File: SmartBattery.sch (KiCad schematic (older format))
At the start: 12 parts, among them J16 Conn_01x03_Female, J17 Conn_01x03_Female, J18 Conn_01x03_Female, J2 ST-USB-003A, Q22 AO3401A, U13 TPS2511DGNR, U14 HT7533-1

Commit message: Type_A_implemented. Sch "locked". PCB Layout started.
*Changelog:
*Type-a switching regulator (TBD -- need to check inductor,caps, stability. Maybe check both peripherial inductors?)
*Type-A load switch + connector + esd
*started layout..
*found out that my footprint for n fet is wrong. Fixing now, need to replace all of those.
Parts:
- removed J16, J17, J18: Conn_01x03_Female, symbol Connector:Conn_01x03_Female
- removed J2: ST-USB-003A, Connector_USB:USB3_A_Plug_Wuerth_692112030100_Horizontal, symbol Connector:USB_B
- removed U13: TPS2511DGNR, SmartBattery:SOP65P490X110-9N, symbol SmartBattery:TPS2511DGNR
- added H1, H2, H3: MountingHole, SmartBattery:MountingHole_1.152mm_JLPCB, symbol Mechanical:MountingHole
- added H4, H5, H6: MountingHole, MountingHole:MountingHole_2.2mm_M2, symbol Mechanical:MountingHole
- added J12: Conn_01x10_Male, Connector_PinHeader_1.27mm:PinHeader_2x05_P1.27mm_Vertical_SMD, symbol Connector:Conn_01x10_Male
- added J?: Conn_01x03_Male, Connector_PinHeader_2.54mm:PinHeader_1x03_P2.54mm_Vertical, symbol Connector:Conn_01x03_Male
- added TP46, TP47, TP48, TP49, TP50, TP51, TP55: TestPoint_Flag, TestPoint:TestPoint_Pad_3.0x3.0mm, symbol Connector:TestPoint_Flag
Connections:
- wire segments 22 -> 20

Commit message: Much layout. Wow
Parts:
- gave numbers to parts that had none: 1
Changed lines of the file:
@@
 $EndComp
 $Comp
-L Connector:Conn_01x03_Male J?
+L Connector:Conn_01x03_Male J13
 U 1 1 604AF604
 P 5300 2300
-F 0 "J?" H 5408 2581 50  0000 C CNN
+F 0 "J13" H 5408 2581 50  0000 C CNN
 F 1 "Conn_01x03_Male" H 5408 2490 50  0000 C CNN
 F 2 "Connector_PinHeader_2.54mm:PinHeader_1x03_P2.54mm_Vertical" H 5300 2300 50  0001 C CNN

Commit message: Much layout wow.
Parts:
- removed J12: Conn_01x10_Male, Connector_PinHeader_1.27mm:PinHeader_2x05_P1.27mm_Vertical_SMD, symbol Connector:Conn_01x10_Male
- added R110, R62, R63: 100k, lc_lib:0402_R, symbol Device:R_Small_US
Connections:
- net Barrel_Jack_Input/BARREL_RAW: now also D12.2 (A)
- net GND: now also C112.1, C113.1, U14.1 (GND), R62.2
- net at U14.2 (VIN): now also C112.2, D12.1 (K), D14.1 (K)
- net at U14.3 (VOUT): now also C113.2, D13.2 (A)
- net +3.3VP: now reaches D13.1 (K)
- net +3.3VP: now also Q22.2 (S), R110.2
- net type_c_input/INPUT_TYPEC_VBUS_RAW: now reaches D14.2 (A)
- net at Q22.1 (G): now also R110.1
- net Peripheral_3p3v/3p3v: now reaches Q22.3 (D)
- new net: R62.1, R63.1
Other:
- note added: "TOOLING HOLE\n"
- note added: "m.2 hole\n"
- moved on the sheet: C112, C113, D12, D13, D14, Q22, U14

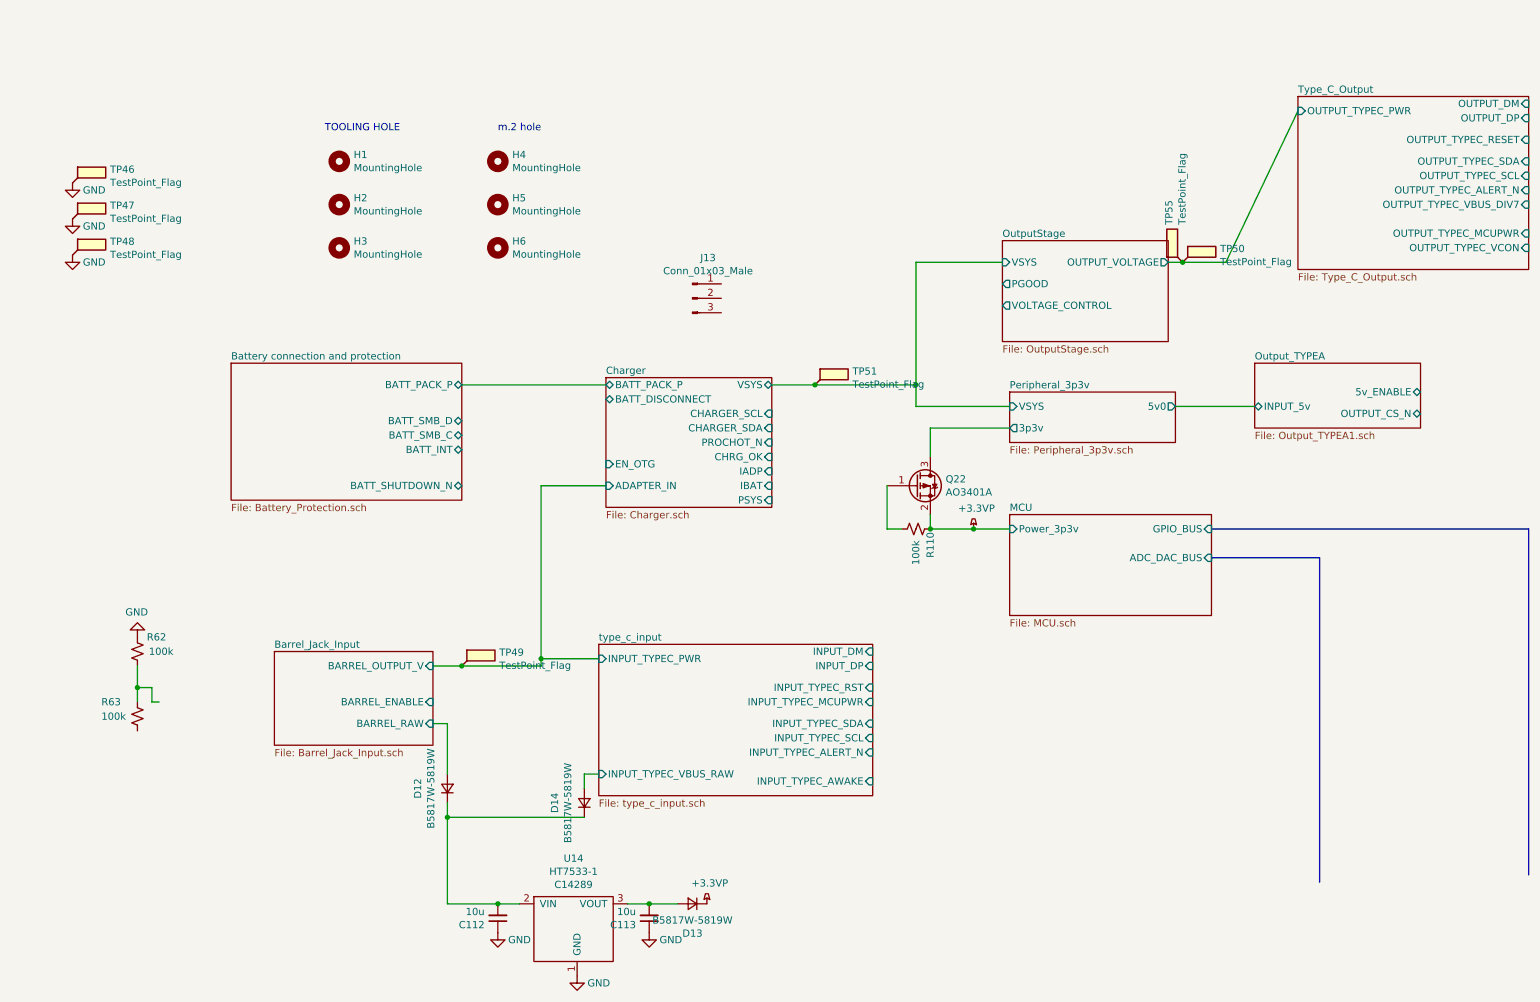
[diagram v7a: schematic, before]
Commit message: Almost connected MCU + ESP32 added leds addedd uart usb cleaned up type-c I/O -- STILL NEED TO level shift I2C
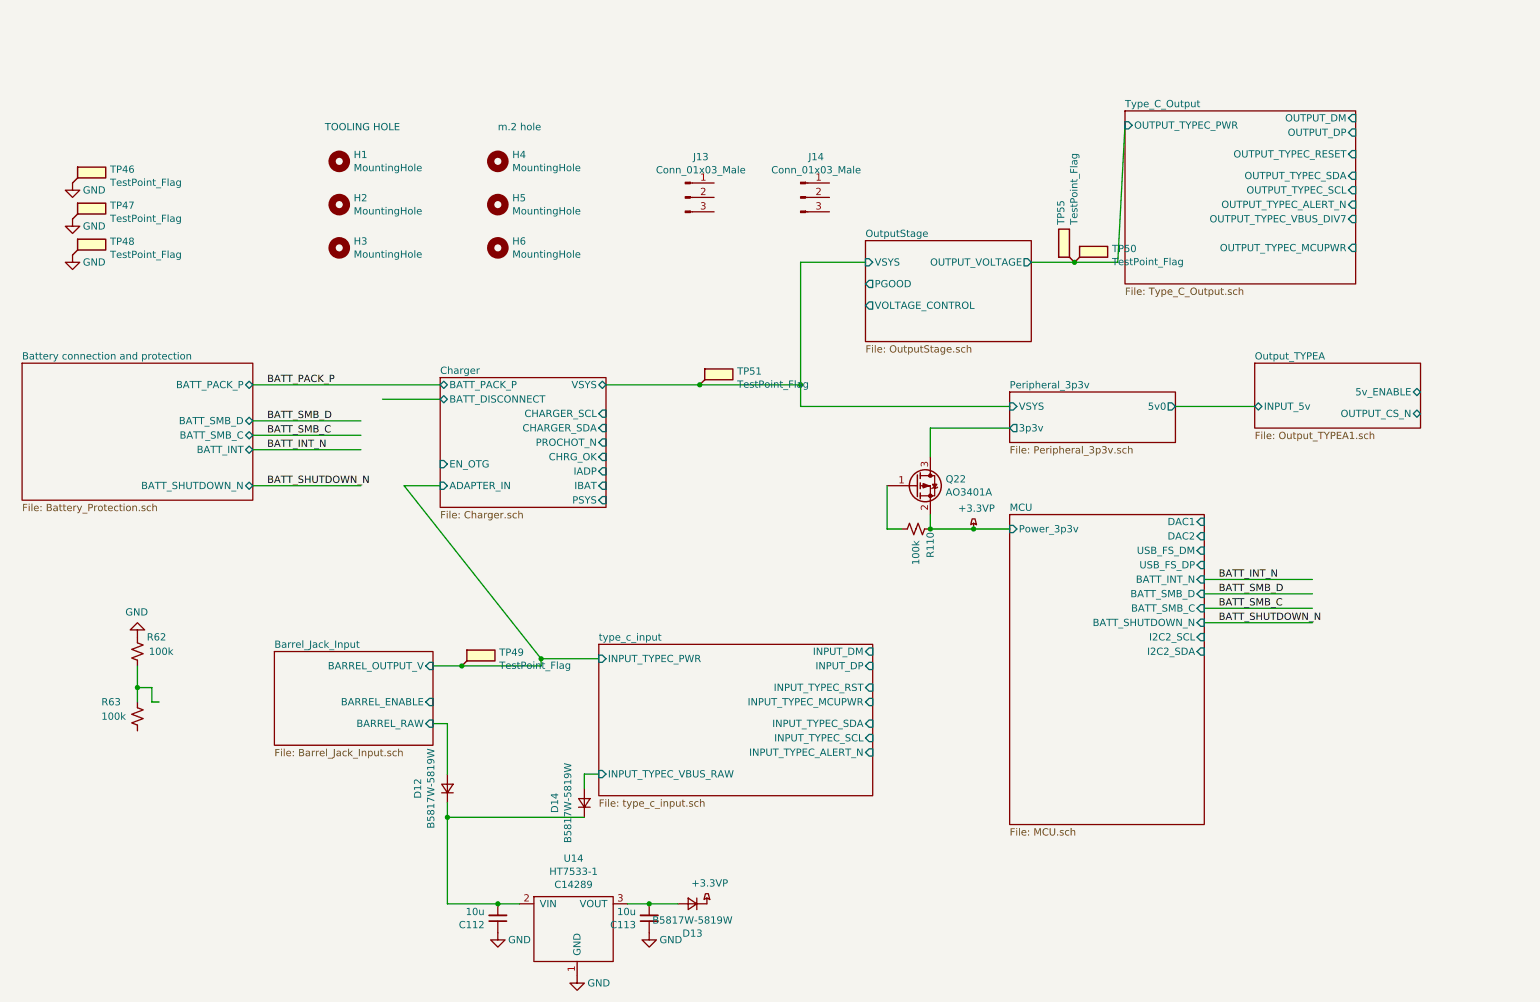
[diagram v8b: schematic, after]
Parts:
- added J14: Conn_01x03_Male, Connector_PinHeader_2.54mm:PinHeader_1x03_P2.54mm_Vertical, symbol Connector:Conn_01x03_Male
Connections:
- net labels added: BATT_INT_N, BATT_PACK_P, BATT_SHUTDOWN_N, BATT_SMB_C, BATT_SMB_D
- wire segments 40 -> 49
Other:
- moved on the sheet: J13, TP50, TP51, TP55
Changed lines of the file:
@@
 $EndDescr
 $Sheet
-S 4700 2850 1150 900
+S 3550 2850 1150 900
 U 5FD99B08
 F0 "Charger" 50
 F1 "Charger.sch" 50
-F2 "BATT_PACK_P" B L 4700 2900 50
-F3 "VSYS" B R 5850 2900 50
-F4 "IBAT" I R 5850 3600 50
-F5 "IADP" I R 5850 3500 50
-F6 "PROCHOT_N" I R 5850 3300 50
-F7 "CHARGER_SDA" I R 5850 3200 50
-F8 "CHARGER_SCL" I R 5850 3100 50
-F9 "ADAPTER_IN" I L 4700 3600 50
-F10 "PSYS" I R 5850 3700 50
-F11 "CHRG_OK" I R 5850 3400 50
-F12 "EN_OTG" I L 4700 3450 50
-F13 "BATT_DISCONNECT" B L 4700 3000 50
-$EndSheet
-$Sheet
-S 7450 1900 1150 700
+F2 "BATT_PACK_P" B L 3550 2900 50
+F3 "VSYS" B R 4700 2900 50
+F4 "IBAT" I R 4700 3600 50
+F5 "IADP" I R 4700 3500 50
+F6 "PROCHOT_N" I R 4700 3300 50
+F7 "CHARGER_SDA" I R 4700 3200 50
+F8 "CHARGER_SCL" I R 4700 3100 50
+F9 "ADAPTER_IN" I L 3550 3600 50
+F10 "PSYS" I R 4700 3700 50
+F11 "CHRG_OK" I R 4700 3400 50
+F12 "EN_OTG" I L 3550 3450 50
+F13 "BATT_DISCONNECT" B L 3550 3000 50
+$EndSheet
+$Sheet
+S 6500 1900 1150 700
 U 60413DD6
 F0 "OutputStage" 50
 F1 "OutputStage.sch" 50
-F2 "VSYS" I L 7450 2050 50
-F3 "OUTPUT_VOLTAGE" O R 8600 2050 50
-F4 "PGOOD" O L 7450 2200 50
-F5 "VOLTAGE_CONTROL" O L 7450 2350 50
+F2 "VSYS" I L 6500 2050 50
+F3 "OUTPUT_VOLTAGE" O R 7650 2050 50
+F4 "PGOOD" O L 6500 2200 50
+F5 "VOLTAGE_CONTROL" O L 6500 2350 50
 $EndSheet
 $Sheet
@@
 $EndSheet
 $Sheet
-S 7500 3800 1400 700
+S 7500 3800 1350 2150
 U 5FF1D194
 F0 "MCU" 50
 F1 "MCU.sch" 50
 F2 "Power_3p3v" I L 7500 3900 50
-F3 "GPIO_BUS" I R 8900 3900 50
-F4 "ADC_DAC_BUS" I R 8900 4100 50
-$EndSheet
-Wire Wire Line
-	6850 2900 6850 3050
-Wire Wire Line
-	6850 3050 7500 3050
-Wire Wire Line
-	5850 2900 6150 2900
+F3 "DAC1" I R 8850 3850 50
+F4 "DAC2" I R 8850 3950 50
+F5 "USB_FS_DM" I R 8850 4050 50
+F6 "USB_FS_DP" I R 8850 4150 50
+F7 "BATT_INT_N" I R 8850 4250 50
+F8 "BATT_SMB_D" I R 8850 4350 50
+F9 "BATT_SMB_C" I R 8850 4450 50
+F10 "BATT_SHUTDOWN_N" I R 8850 4550 50
+F11 "I2C2_SCL" I R 8850 4650 50
+F12 "I2C2_SDA" I R 8850 4750 50
+$EndSheet
+Wire Wire Line
+	6050 2900 6050 3050
+Wire Wire Line
+	4700 2900 5350 2900
 Wire Wire Line
 	6950 3200 7500 3200
 Wire Wire Line
-	6850 2900 6850 2050
-Wire Wire Line
-	6850 2050 7450 2050
-Connection ~ 6850 2900
+	6050 2900 6050 2050
+Connection ~ 6050 2900
 $Comp
 L power:GND #PWR0159
@@
 $EndComp
 Wire Wire Line
-	8600 2050 8700 2050
+	7650 2050 7950 2050
 Wire Wire Line
 	6950 3900 7250 3900
@@
 	6950 3900 6950 3800
 $Sheet
-S 9500 900  1600 1200
+S 8300 1000 1600 1200
 U 600C8F88
 F0 "Type_C_Output" 50
 F1 "Type_C_Output.sch" 50
-F2 "OUTPUT_DM" I R 11100 950 50
-F3 "OUTPUT_DP" I R 11100 1050 50
-F4 "OUTPUT_TYPEC_SDA" I R 11100 1350 50
-F5 "OUTPUT_TYPEC_SCL" I R 11100 1450 50
-F6 "OUTPUT_TYPEC_ALERT_N" I R 11100 1550 50
-F7 "OUTPUT_TYPEC_VBUS_DIV7" I R 11100 1650 50
-F8 "OUTPUT_TYPEC_PWR" I L 9500 1000 50
-F9 "OUTPUT_TYPEC_MCUPWR" I R 11100 1850 50
-F10 "OUTPUT_TYPEC_RESET" I R 11100 1200 50
-F11 "OUTPUT_TYPEC_VCON" I R 11100 1950 50
-$EndSheet
-Wire Wire Line
-	4250 3600 4700 3600
+F2 "OUTPUT_DM" I R 9900 1050 50
+F3 "OUTPUT_DP" I R 9900 1150 50
+F4 "OUTPUT_TYPEC_SDA" I R 9900 1450 50
+F5 "OUTPUT_TYPEC_SCL" I R 9900 1550 50
+F6 "OUTPUT_TYPEC_ALERT_N" I R 9900 1650 50
+F7 "OUTPUT_TYPEC_VBUS_DIV7" I R 9900 1750 50
+F8 "OUTPUT_TYPEC_PWR" I L 8300 1100 50
+F9 "OUTPUT_TYPEC_MCUPWR" I R 9900 1950 50
+F10 "OUTPUT_TYPEC_RESET" I R 9900 1300 50
+$EndSheet
+Wire Wire Line
+	3300 3600 3550 3600
 Wire Wire Line
 	3500 4850 3700 4850
@@
 	4250 4800 4650 4800
 Wire Wire Line
-	9000 2050 9500 1000
+	8250 2050 8300 1100
 $Sheet
 S 2400 4750 1100 650
@@
 L Connector:TestPoint_Flag TP51
 U 1 1 60166682
-P 6150 2900
-F 0 "TP51" H 6410 2994 50  0000 L CNN
-F 1 "TestPoint_Flag" H 6410 2903 50  0000 L CNN
-F 2 "TestPoint:TestPoint_Pad_3.0x3.0mm" H 6350 2900 50  0001 C CNN
-F 3 "~" H 6350 2900 50  0001 C CNN
-	1    6150 2900
-	1    0    0    -1
-$EndComp
-Connection ~ 6150 2900
-Wire Wire Line
-	6150 2900 6850 2900
+P 5350 2900
+F 0 "TP51" H 5610 2994 50  0000 L CNN
+F 1 "TestPoint_Flag" H 5610 2903 50  0000 L CNN
+F 2 "TestPoint:TestPoint_Pad_3.0x3.0mm" H 5550 2900 50  0001 C CNN
+F 3 "~" H 5550 2900 50  0001 C CNN
+	1    5350 2900
+	1    0    0    -1
+$EndComp
+Connection ~ 5350 2900
+Wire Wire Line
+	5350 2900 6050 2900
 $Sheet
 S 9200 2750 1150 450
@@
 L Connector:TestPoint_Flag TP50
 U 1 1 60165EDF
-P 8700 2050
-F 0 "TP50" H 8960 2144 50  0000 L CNN
-F 1 "TestPoint_Flag" H 8960 2053 50  0000 L CNN
-F 2 "TestPoint:TestPoint_Pad_3.0x3.0mm" H 8900 2050 50  0001 C CNN
-F 3 "~" H 8900 2050 50  0001 C CNN
-	1    8700 2050
-	1    0    0    -1
-$EndComp
-Connection ~ 8700 2050
-Wire Wire Line
-	8700 2050 9000 2050
+P 7950 2050
+F 0 "TP50" H 8210 2144 50  0000 L CNN
+F 1 "TestPoint_Flag" H 8210 2053 50  0000 L CNN
+F 2 "TestPoint:TestPoint_Pad_3.0x3.0mm" H 8150 2050 50  0001 C CNN
+F 3 "~" H 8150 2050 50  0001 C CNN
+	1    7950 2050
+	1    0    0    -1
+$EndComp
+Connection ~ 7950 2050
+Wire Wire Line
+	7950 2050 8250 2050
 $Comp
 L Connector:TestPoint_Flag TP55
 U 1 1 602EF777
-P 8700 2050
-F 0 "TP55" H 8960 2144 50  0000 L CNN
-F 1 "TestPoint_Flag" H 8960 2053 50  0000 L CNN
-F 2 "TestPoint:TestPoint_Pad_3.0x3.0mm" H 8900 2050 50  0001 C CNN
-F 3 "~" H 8900 2050 50  0001 C CNN
-	1    8700 2050
+P 7950 2050
+F 0 "TP55" H 8210 2144 50  0000 L CNN
+F 1 "TestPoint_Flag" H 8210 2053 50  0000 L CNN
+F 2 "TestPoint:TestPoint_Pad_3.0x3.0mm" H 8150 2050 50  0001 C CNN
+F 3 "~" H 8150 2050 50  0001 C CNN
+	1    7950 2050
 	0    -1   -1   0
 $EndComp
@@
 $EndComp
 Wire Wire Line
-	3700 2900 4700 2900
+	2250 2900 3550 2900
 $Comp
 L Mechanical:MountingHole H5
@@
 L Connector:Conn_01x03_Male J13
 U 1 1 604AF604
-P 5300 2300
-F 0 "J13" H 5408 2581 50  0000 C CNN
-F 1 "Conn_01x03_Male" H 5408 2490 50  0000 C CNN
-F 2 "Connector_PinHeader_2.54mm:PinHeader_1x03_P2.54mm_Vertical" H 5300 2300 50  0001 C CNN
-F 3 "~" H 5300 2300 50  0001 C CNN
-	1    5300 2300
-	1    0    0    -1
-$EndComp
-$Sheet
-S 2100 2750 1600 950
+P 5250 1600
+F 0 "J13" H 5358 1881 50  0000 C CNN
+F 1 "Conn_01x03_Male" H 5358 1790 50  0000 C CNN
+F 2 "Connector_PinHeader_2.54mm:PinHeader_1x03_P2.54mm_Vertical" H 5250 1600 50  0001 C CNN
+F 3 "~" H 5250 1600 50  0001 C CNN
+	1    5250 1600
+	1    0    0    -1
+$EndComp
+$Sheet
+S 650  2750 1600 950
 U 5FD15753
 F0 "Battery connection and protection" 50
 F1 "Battery_Protection.sch" 50
-F2 "BATT_PACK_P" B R 3700 2900 50
-F3 "BATT_SMB_D" B R 3700 3150 50
-F4 "BATT_SMB_C" B R 3700 3250 50
-F5 "BATT_SHUTDOWN_N" B R 3700 3600 50
-F6 "BATT_INT" B R 3700 3350 50
+F2 "BATT_PACK_P" B R 2250 2900 50
+F3 "BATT_SMB_D" B R 2250 3150 50
+F4 "BATT_SMB_C" B R 2250 3250 50
+F5 "BATT_SHUTDOWN_N" B R 2250 3600 50
+F6 "BATT_INT" B R 2250 3350 50
 $EndSheet
 Text Notes 2750 1150 0    50   ~ 0
@@
 F7 "INPUT_TYPEC_ALERT_N" I R 6550 5450 50
 F8 "INPUT_TYPEC_PWR" I L 4650 4800 50
-F9 "INPUT_TYPEC_AWAKE" I R 6550 5650 50
 F10 "INPUT_TYPEC_MCUPWR" I R 6550 5100 50
 F11 "INPUT_TYPEC_VBUS_RAW" I L 4650 5600 50
@@
 	4250 4800 4250 4850
 Wire Wire Line
-	4250 3600 4250 4800
+	3300 3600 4250 4800
 Wire Wire Line
 	4650 5600 4550 5600
@@
 Wire Wire Line
 	6650 3900 6650 3600
-Wire Bus Line
-	8900 3900 11100 3900
-Wire Bus Line
-	8900 4100 9650 4100
-Wire Bus Line
-	9650 4100 9650 6350
-Wire Bus Line
-	11100 3900 11100 6300
+Wire Wire Line
+	2250 3350 3000 3350
+Wire Wire Line
+	2250 3250 3000 3250
+Wire Wire Line
+	2250 3150 3000 3150
+Text Label 2350 3350 0    50   ~ 0
+BATT_INT_N
+Text Label 2350 3250 0    50   ~ 0
+BATT_SMB_C
+Text Label 2350 3150 0    50   ~ 0
+BATT_SMB_D
+Text Label 2350 3600 0    50   ~ 0
+BATT_SHUTDOWN_N
+Wire Wire Line
+	3000 3600 2250 3600
+Text Label 2350 2900 0    50   ~ 0
+BATT_PACK_P
+Wire Wire Line
+	3150 3000 3550 3000
+Wire Wire Line
+	8850 4250 9600 4250
+Wire Wire Line
+	8850 4450 9600 4450
+Wire Wire Line
+	8850 4350 9600 4350
+Text Label 8950 4250 0    50   ~ 0
+BATT_INT_N
+Text Label 8950 4450 0    50   ~ 0
+BATT_SMB_C
+Text Label 8950 4350 0    50   ~ 0
+BATT_SMB_D
+Text Label 8950 4550 0    50   ~ 0
+BATT_SHUTDOWN_N
+Wire Wire Line
+	9600 4550 8850 4550
+Wire Wire Line
+	6050 3050 7500 3050
+Wire Wire Line
+	6050 2050 6500 2050
+$Comp
+L Connector:Conn_01x03_Male J14
+U 1 1 6030B31F
+P 6050 1600
+F 0 "J14" H 6158 1881 50  0000 C CNN
+F 1 "Conn_01x03_Male" H 6158 1790 50  0000 C CNN
+F 2 "Connector_PinHeader_2.54mm:PinHeader_1x03_P2.54mm_Vertical" H 6050 1600 50  0001 C CNN
+F 3 "~" H 6050 1600 50  0001 C CNN
+	1    6050 1600
+	1    0    0    -1
+$EndComp
 $EndSCHEMATC
